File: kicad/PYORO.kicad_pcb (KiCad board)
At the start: 2 copper layers, 90.6 x 88 mm, 119 parts, among them J1 BM06B-SRSS-TBLFSN, J2 Conn_01x04_Pin, J3 BM06B-SRSS-TBLFSN, J4 Conn_01x04_Pin, Q1 TEFT4300, Q2 TEFT4300, Q3 TEFT4300, Q4 TEFT4300, Q5 NMOS, Q6 NMOS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

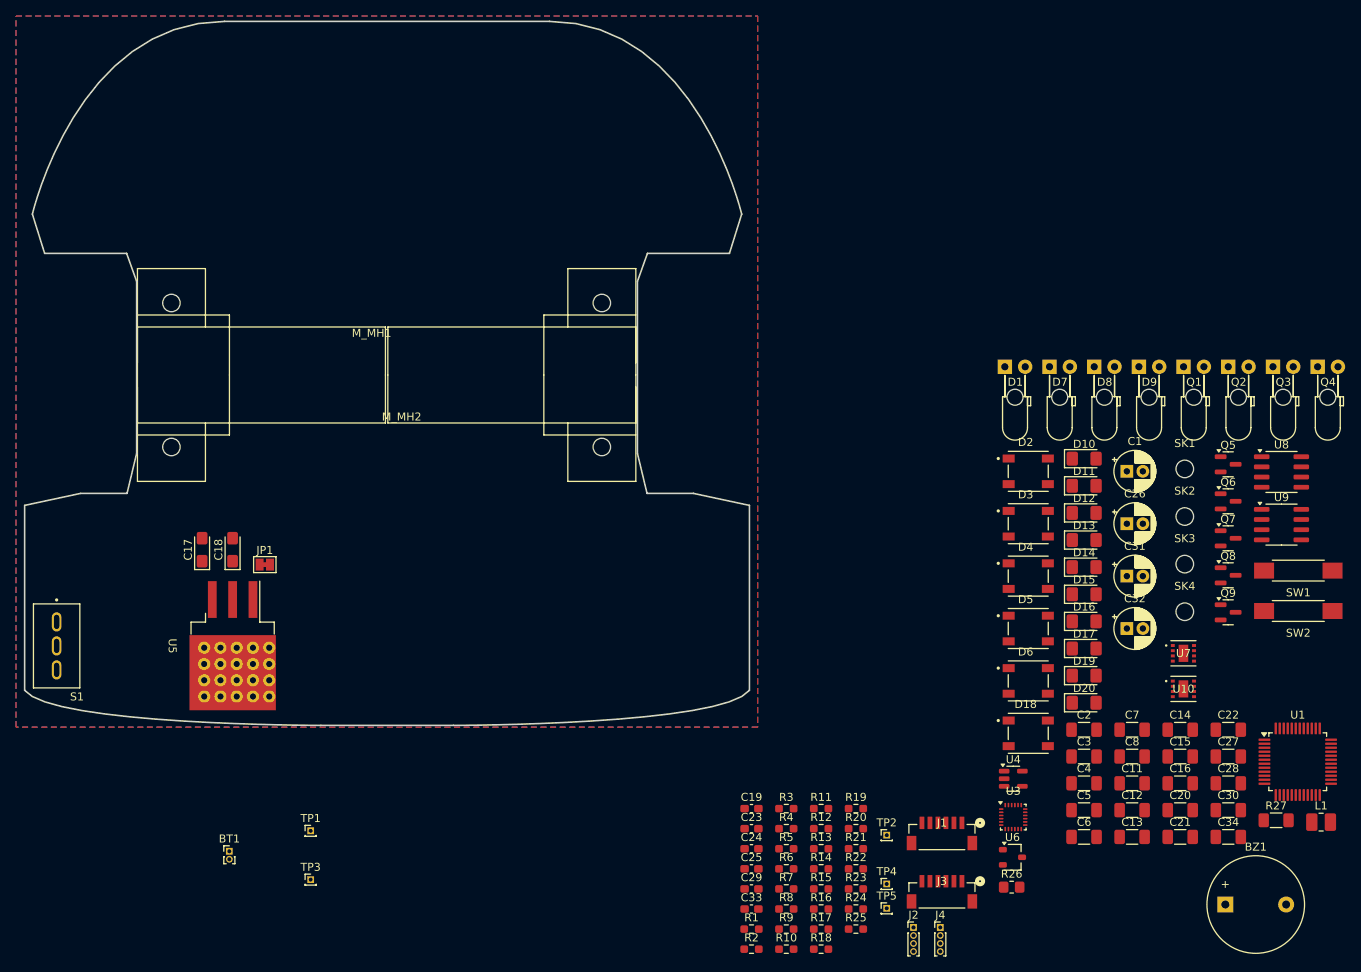
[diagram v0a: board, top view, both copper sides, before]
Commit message: Started Pwr Supply layout
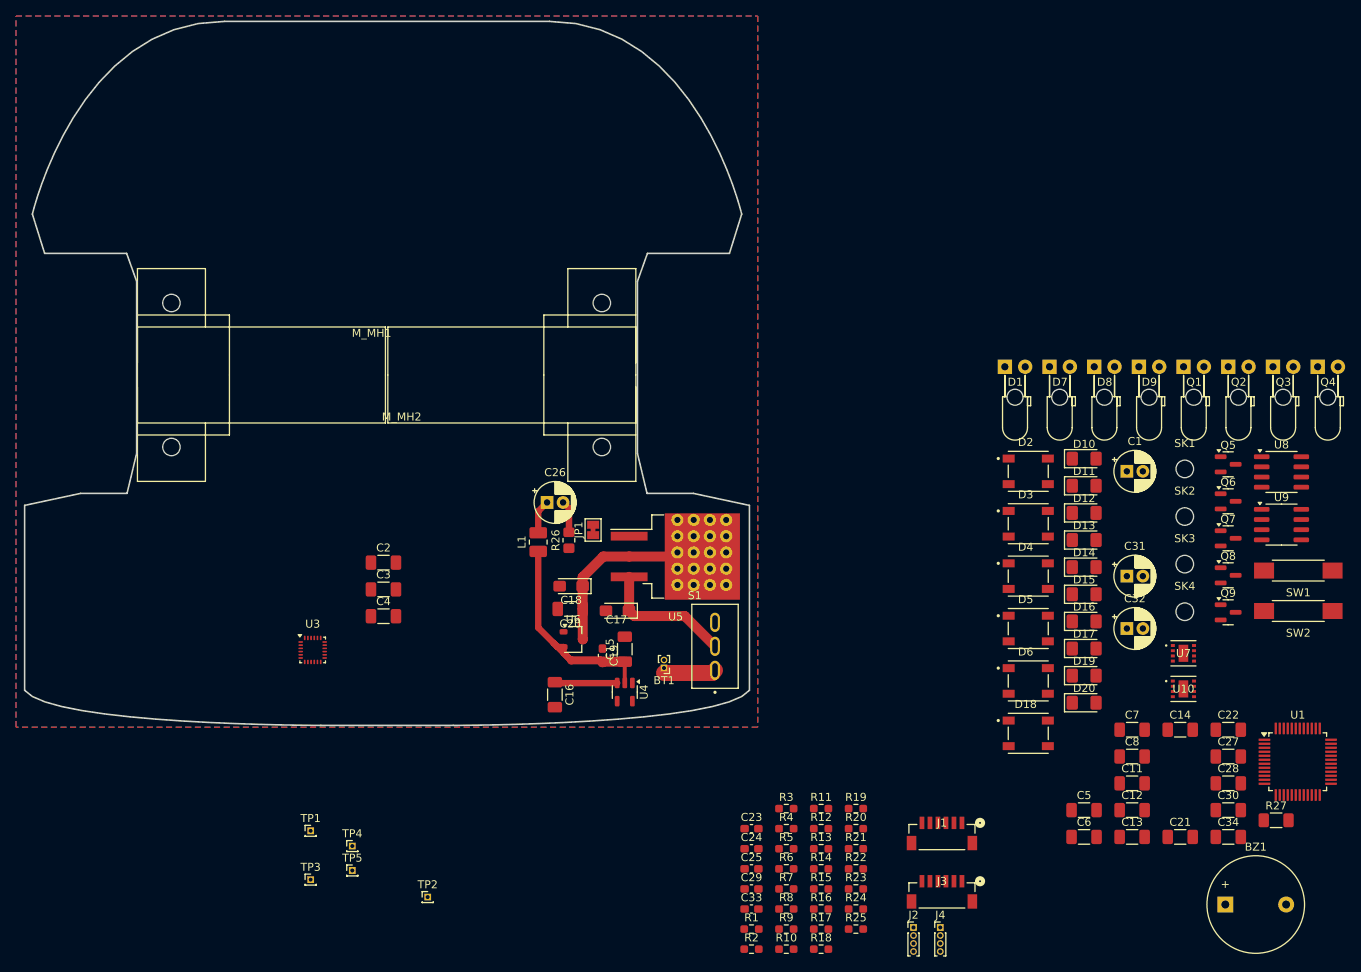
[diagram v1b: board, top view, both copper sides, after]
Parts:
- moved L1 103.9 mm to (85.6, 82.3), turned to 90 degrees
- moved C2 90.0 mm to (66.3, 84.8)
- moved C3 90.0 mm to (66.3, 88.2)
- moved C4 90.0 mm to (66.3, 91.5)
- moved U3 90.0 mm to (57.4, 95.8)
- moved S1 82.3 mm to (107.7, 95.3), turned to 90 degrees
- moved C20 80.3 mm to (89.6, 90.6), turned to 180 degrees
- moved C16 78.9 mm to (87.7, 101.3), turned to -90 degrees
- moved C26 72.5 mm to (86.7, 77.3)
- moved C15 70.7 mm to (96.4, 95.7), turned to 90 degrees
- moved R26 70.3 mm to (89.4, 82.0), turned to 90 degrees
- moved TP4 67.0 mm to (62.4, 120.3)
- moved TP5 67.0 mm to (62.4, 123.3)
- moved U5 63.5 mm to (102.8, 92.1), turned to 0 degrees
- moved U6 61.3 mm to (90.0, 94.4)
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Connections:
- net /5V_REG_IN renamed /REG5V_IN
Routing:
- net +3V3: track 0.00 -> 28.4 mm
- net +5V: track 0.00 -> 23.8 mm
- net /REG5V_IN: track 0.00 -> 16.8 mm
- net +1V8: track 0.00 -> 7.85 mm
- net /BATT_PIN: track 0.00 -> 6.52 mm
- net Net-(C26-Pad1): track 0.00 -> 4.25 mm
- net +3.3VA: track 0.00 -> 4.04 mm

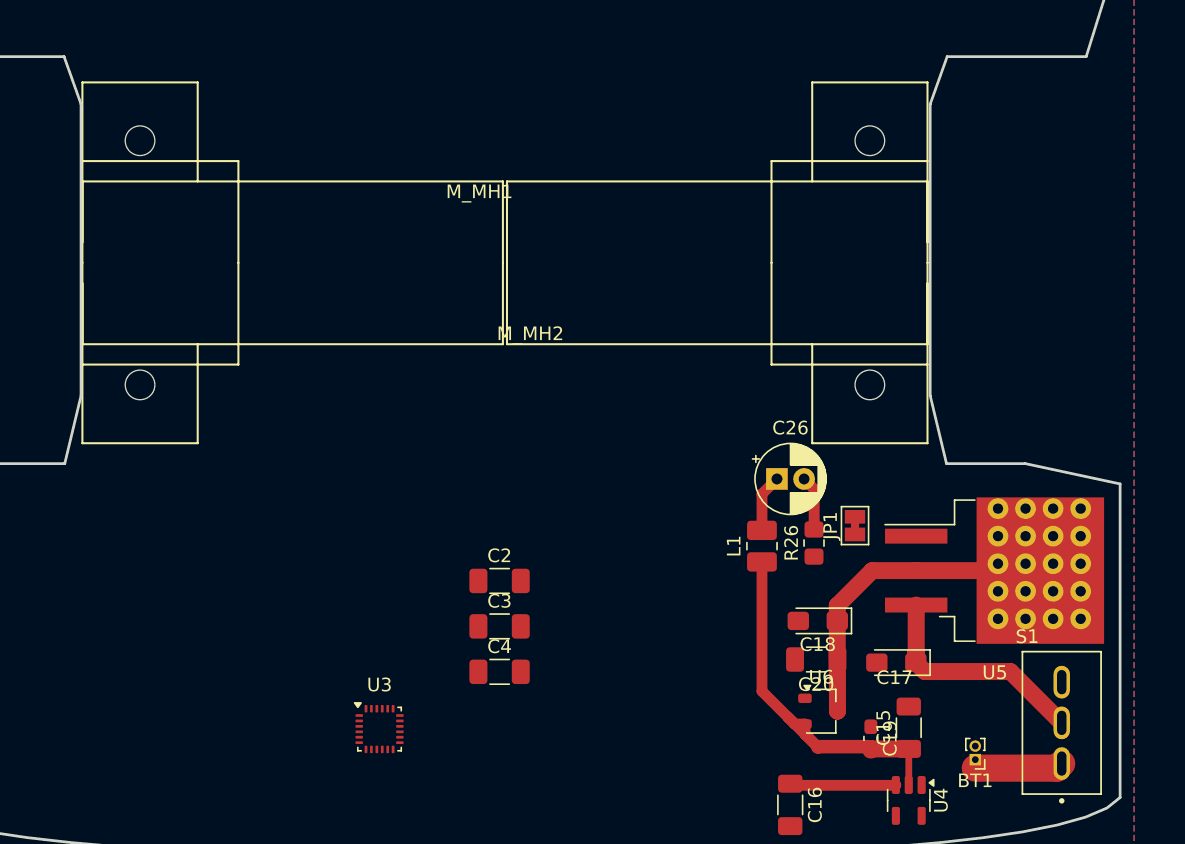
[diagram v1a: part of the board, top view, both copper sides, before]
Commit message: Changed graphic fonts
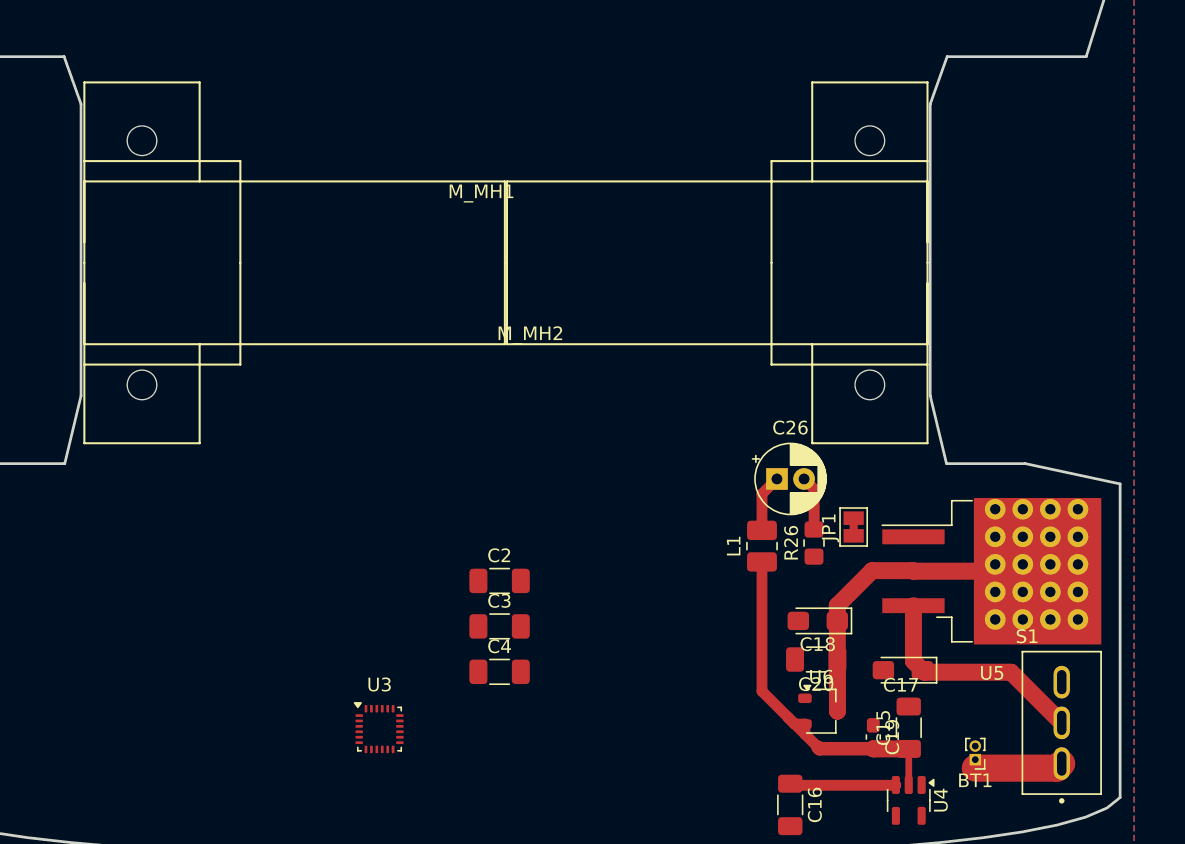
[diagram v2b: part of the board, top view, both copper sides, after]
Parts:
- moved C17 0.74 mm to (96.0, 91.4)
- moved U5 0.21 mm to (102.6, 92.2)
- moved C19 0.20 mm to (93.8, 96.3)
- moved M_MH1 0.14 mm to (66.6, 61.4)
- moved JP1 0.14 mm to (92.4, 80.9)
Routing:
- net +3V3: track 28.4 -> 27.0 mm
